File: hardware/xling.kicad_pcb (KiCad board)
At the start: 2 copper layers, 51 x 68 mm, 59 parts, among them J2 TPS63031, J3 MCP73831, J4 USB_OTG, J5 AVR ISP, J6 Battery, Q1 TP0610T, SW1 Reset, SW2 Up, SW3 Select, SW4 Down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

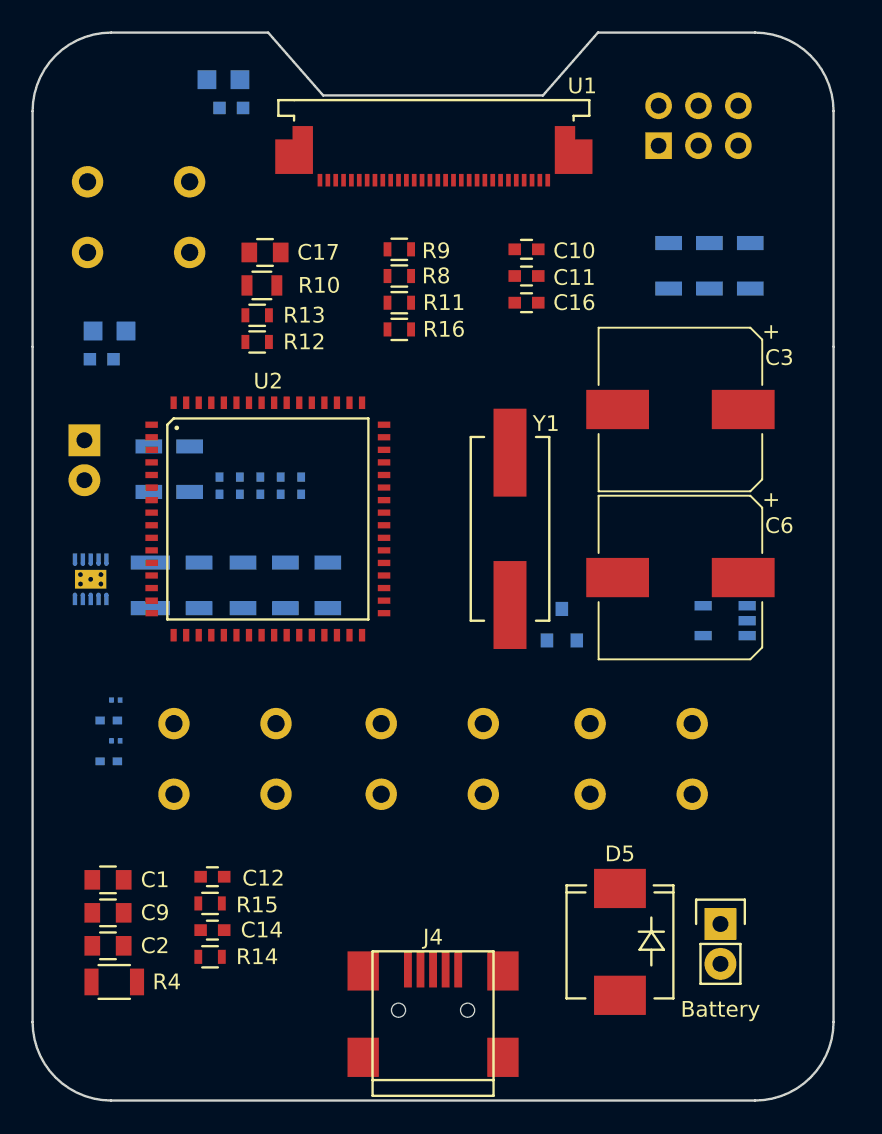
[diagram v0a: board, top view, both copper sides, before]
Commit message: patch 0.1.8: Add other OLED and DCDC 3V-to-12V.
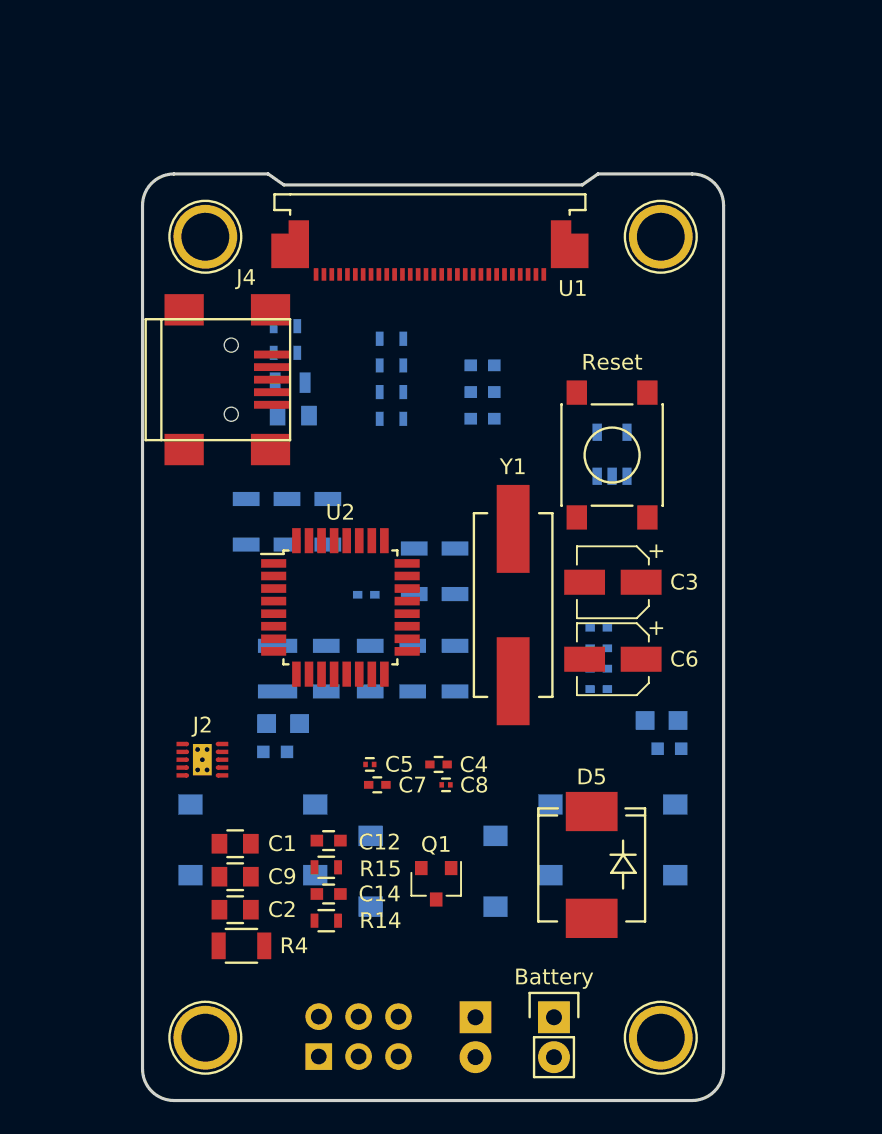
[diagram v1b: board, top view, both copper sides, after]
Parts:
- added REF**: 1pin, Connectors:1pin, F.Cu at (123.0, 134.0)
- added REF**: 1pin, Connectors:1pin, F.Cu at (152.0, 134.0)
- added REF**: 1pin, Connectors:1pin, F.Cu at (123.0, 83.0)
- added REF**: 1pin, Connectors:1pin, F.Cu at (152.0, 83.0)
- C10, C11, C16, C17, R10, R11, R12, R13, R16, R8, R9: moved to B.Cu
- C3, C6: footprint Capacitors_SMD:CP_Elec_10x10 -> Capacitors_SMD:CP_Elec_4x5.3
- C4, C5, C7, C8, J2, Q1: moved to F.Cu
- J5: footprint Socket_Strips:Socket_Strip_Angled_2x03_Pitch2.54mm -> Socket_Strips:Socket_Strip_Straight_2x03_Pitch2.54mm
- SW1: footprint Buttons_Switches_THT:SW_PUSH_6mm -> Buttons_Switches_SMD:SW_SPST_PTS645; moved to F.Cu
- SW2, SW3, SW4: footprint Buttons_Switches_THT:SW_PUSH_6mm -> Buttons_Switches_SMD:SW_SPST_PTS645
- U2: value ATMEGA128-16AU -> ATMEGA328P-AU; footprint Xling Footprints:ATmega128_64-lead_14x14x1.0mm_TQFP -> Housings_QFP:TQFP-32_7x7mm_Pitch0.8mm
- moved J5 61.9 mm to (130.2, 135.2)
- moved D1 49.4 mm to (152.6, 115.6)
- moved D2 49.4 mm to (152.1, 113.8)
- moved JP1 44.4 mm to (140.2, 132.7)
- moved J4 43.2 mm to (123.8, 92.1), turned to 0 degrees
- moved SW1 32.0 mm to (148.9, 96.9), turned to 90 degrees
- moved R3 31.5 mm to (128.2, 101.2)
- moved R6 31.5 mm to (125.6, 101.2)
- moved R7 31.5 mm to (130.8, 101.2)
- moved D3 27.3 mm to (128.0, 114.0)
- moved D4 27.3 mm to (127.5, 115.8)
- moved C15 26.3 mm to (148.1, 111.8), turned to 180 degrees
- moved C18 24.5 mm to (148.1, 110.5), turned to 180 degrees
- moved C19 22.7 mm to (148.1, 109.2), turned to 180 degrees
- moved C8 21.2 mm to (138.3, 117.9)
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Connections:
- R8 pad 2: /OLED_SCL -> /OLED_SDA
- R9 pad 2: /OLED_SDA -> /OLED_SCL
- U2 pad 11: /ISP_SCK -> Net-(U2-Pad11)
- U2 pad 15: Net-(U2-Pad15) -> /ISP_PDI_MOSI
- U2 pad 16: Net-(U2-Pad16) -> /ISP_PDO_MISO
- U2 pad 17: Net-(U2-Pad17) -> /ISP_SCK
- U2 pad 18: Net-(U2-Pad18) -> +3V3
- U2 pad 2: Net-(R11-Pad1) -> Net-(U2-Pad2)
- U2 pad 20: /ISP_RST -> GND
- U2 pad 21: +3V3 -> GND
- U2 pad 22: GND -> Net-(U2-Pad22)
- U2 pad 23: Net-(C13-Pad1) -> Net-(U2-Pad23)
- U2 pad 24: Net-(C15-Pad1) -> Net-(U2-Pad24)
- U2 pad 25: /OLED_SCL -> Net-(U2-Pad25)
- U2 pad 26: /OLED_SDA -> Net-(U2-Pad26)
- U2 pad 27: Net-(U2-Pad27) -> /OLED_SDA
- U2 pad 28: Net-(U2-Pad28) -> /OLED_SCL
- U2 pad 29: Net-(U2-Pad29) -> /ISP_RST
- U2 pad 3: /ISP_PDO_MISO -> GND
- U2 pad 30: Net-(U2-Pad30) -> /BTN1
- U2 pad 31: Net-(U2-Pad31) -> /BTN2
- U2 pad 32: Net-(U2-Pad32) -> /BTN3
- U2 pad 4: Net-(U2-Pad4) -> +3V3
- U2 pad 5: Net-(U2-Pad5) -> GND
- U2 pad 6: Net-(D3-Pad1) -> +3V3
- U2 pad 7: Net-(D4-Pad1) -> Net-(C13-Pad1)
- U2 pad 8: Net-(U2-Pad8) -> Net-(C15-Pad1)
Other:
- board size 51 x 68 mm -> 37 x 59 mm
- net class Default: clearance 0.25 -> 0.21
- rule trace_clearance: 0.25 -> 0.21
- rule trace_min: 0.2 -> 0.25
- rule via_min_size: 0.4 -> 0.6

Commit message: patch 0.1.10: First PCB prototype.
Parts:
- removed C14, C16: 2.2uF, Capacitors_SMD:C_0603
- removed C17, C2, C9: 10uF, Capacitors_SMD:C_0805
- removed C4: 10nF, Capacitors_SMD:C_0402
- removed D4: amber, LEDs:LED_0603
- removed J2: TPS63031, Xling Footprints:TPS63031_QFN_10
- removed JP1: D2D1, Pin_Headers:Pin_Header_Straight_1x02
- removed R10: 174K, Resistors_SMD:R_0805
- removed R11, R12, R13: 1K, Resistors_SMD:R_0603
- removed the REF** at (152.0, 134.0)
- removed the REF** at (123.0, 83.0)
- removed the REF** at (152.0, 83.0)
- removed SW1: Reset, Buttons_Switches_SMD:SW_SPST_PTS645
- added L2: 22uH, Inductors_SMD:L_7.3x7.3_H3.5, F.Cu at (127.1, 115.2)
- added REF**: 1pin, Connectors:1pin, F.Cu at (160.0, 134.0)
- added REF**: 1pin, Connectors:1pin, F.Cu at (160.0, 82.0)
- added REF**: 1pin, Connectors:1pin, F.Cu at (123.0, 82.0)
- added U3: DEP_128064I, Xling Footprints:XF2M_24151AR100_SMD_1x24_Pitch_0.5mm, F.Cu at (141.5, 81.2)
- added U4: MCP1640B-CH, TO_SOT_Packages_SMD:SOT-23-6, B.Cu at (141.7, 93.0)
- C1, J4, Q1: moved to B.Cu
- C10: value 2.2uF -> 33uF; footprint Capacitors_SMD:C_0603 -> Capacitors_Tantalum_SMD:CP_Tantalum_Case-C_EIA-6032-28_Reflow; moved to F.Cu
- C11, C13, J3, J5, R1, R16, R3, R5, R9: moved to F.Cu
- C5: value 0.1uF -> 4.7uF; moved to B.Cu
- D3: value green -> 1N5818; footprint LEDs:LED_0805 -> Diodes_THT:D_DO-41_SOD81_P7.62mm_Horizontal; moved to F.Cu
- D5: value B320 -> 1N5818; footprint Diodes_SMD:SMC_Standard -> Diodes_THT:D_DO-41_SOD81_P7.62mm_Horizontal
- L1: value 1.5uH -> 4.7uH
- R2: value 100K -> 910K
- R6: value 10K -> 191K; footprint Resistors_SMD:R_1206 -> Resistors_SMD:R_0805
- R7: value 10K -> 110K; footprint Resistors_SMD:R_1206 -> Resistors_SMD:R_0805
- U1: value SH1106G -> LT1109CZ-12; footprint Xling Footprints:Connector_FFC_FPC_MOLEX_524353071_30-pins -> TO_SOT_Packages_THT:TO-92_Inline_Narrow_Oval
- moved J5 47.9 mm to (152.4, 92.8), turned to 0 degrees
- moved J4 44.6 mm to (141.5, 133.0), turned to 90 degrees
- moved D5 36.2 mm to (156.8, 88.0)
- moved C1 35.0 mm to (145.1, 93.1), turned to 90 degrees
- moved R3 27.9 mm to (154.2, 111.2), turned to 180 degrees
- moved C18 26.0 mm to (127.5, 94.6)
- moved C19 24.3 mm to (127.5, 96.4)
- moved C5 23.9 mm to (138.8, 93.3), turned to 90 degrees
- moved R16 21.6 mm to (138.3, 110.8)
- moved C15 21.4 mm to (127.5, 105.9)
- moved D3 21.0 mm to (130.4, 93.1), turned to 90 degrees
- moved R1 20.7 mm to (159.2, 100.3), turned to 180 degrees
- moved R6 19.5 mm to (144.8, 97.6), turned to 180 degrees
- moved R14 19.1 mm to (149.3, 122.2)
- moved L1 19.1 mm to (136.0, 93.4)
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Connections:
- C10 pad 1: Net-(C10-Pad1) -> +12V
- C10 pad 2: Net-(C10-Pad2) -> GND
- C11 pad 2: Net-(C11-Pad2) -> GND
- C12 pad 1: +3V3 -> +12V
- D3 pad 1: Net-(D3-Pad1) -> +12V
- D5 pad 1: Net-(D5-Pad1) -> Net-(C5-Pad1)
- L1 pad 1: Net-(J2-Pad4) -> Net-(C5-Pad1)
- Q1 pad 2: Net-(D5-Pad1) -> Net-(C5-Pad1)
- R2 pad 1: Net-(C4-Pad1) -> GND
- R2 pad 2: Net-(D5-Pad1) -> Net-(R2-Pad2)
- R6 pad 2: /ISP_RST -> Net-(R6-Pad2)
- R7 pad 1: +3V3 -> Net-(R6-Pad2)
- U1 pad 2: Net-(C10-Pad1) -> Net-(D3-Pad2)
- U1 pad 3: Net-(C10-Pad2) -> +12V
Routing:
- net GND: track 0.00 -> 368.6 mm, vias 0 -> 15
- net +3V3: track 0.00 -> 134.9 mm, vias 0 -> 7
- net +12V: track 0.00 -> 84.2 mm, vias 0 -> 6
- net Net-(C3-Pad1): track 0.00 -> 75.7 mm, vias 0 -> 1
- net /ISP_RST: track 0.00 -> 48.4 mm, vias 0 -> 2
- net Net-(C5-Pad1): track 0.00 -> 46.7 mm
- net /ISP_PDO_MISO: track 0.00 -> 44.5 mm, vias 0 -> 2
- net Net-(R14-Pad2): track 0.00 -> 43.5 mm, vias 0 -> 3
- net /ISP_SCK: track 0.00 -> 38.9 mm, vias 0 -> 2
- net Net-(C6-Pad1): track 0.00 -> 37.7 mm, vias 0 -> 1
- net Net-(R15-Pad2): track 0.00 -> 37.6 mm, vias 0 -> 2
- net /OLED_SDA: track 0.00 -> 33.3 mm, vias 0 -> 1
- net Net-(D3-Pad2): track 0.00 -> 33.2 mm
- net Net-(R16-Pad2): track 0.00 -> 32.5 mm, vias 0 -> 3
- net Net-(R2-Pad2): track 0.00 -> 31.8 mm, vias 0 -> 1
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- added copper zone on B.Cu, net +3V3
- added copper zone on B.Cu, net GND
- added copper zone on F.Cu, net GND
- added copper zone on F.Cu, net Net-(C3-Pad1)
- added copper zone on B.Cu, net Net-(C5-Pad1)
- added copper zone on F.Cu, net Net-(C6-Pad1)
- added copper zone on B.Cu, net Net-(L1-Pad2)
- added copper zone on B.Cu, net Net-(R6-Pad2)
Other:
- board size 37 x 59 mm -> 45 x 60 mm

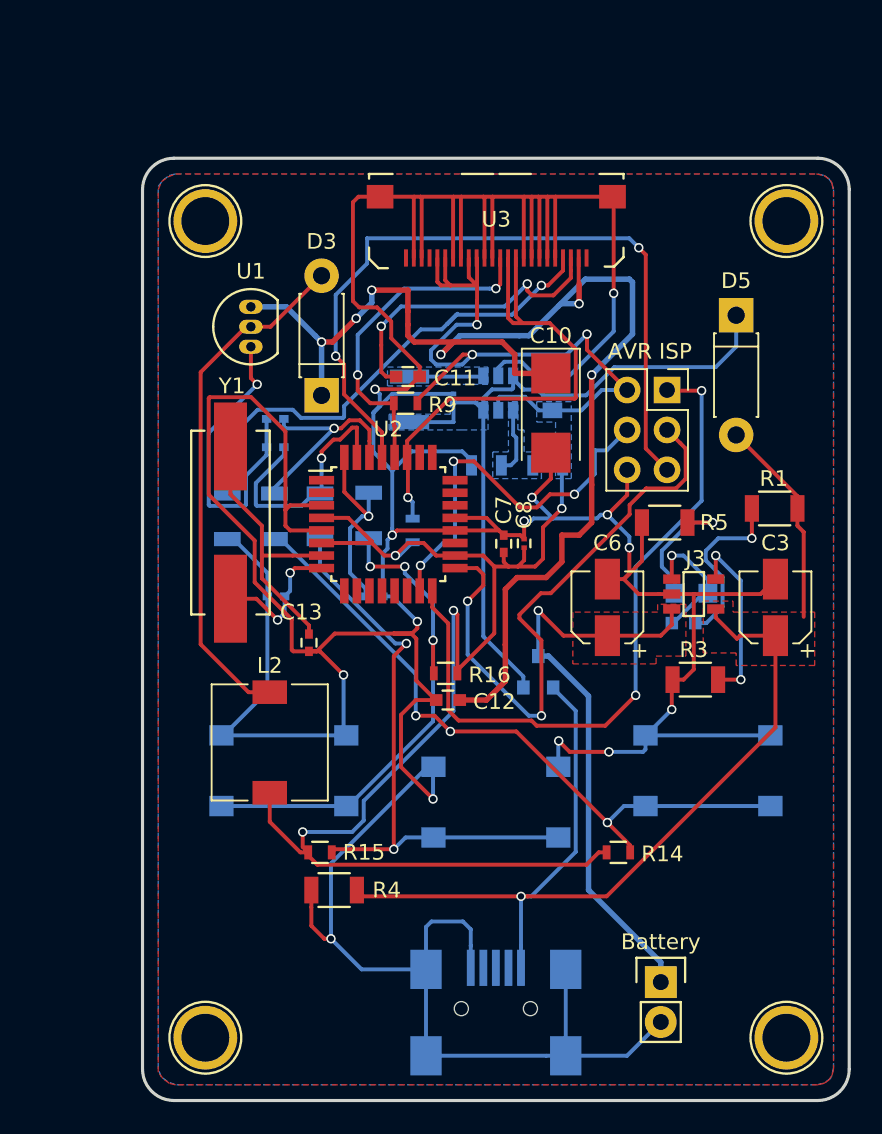
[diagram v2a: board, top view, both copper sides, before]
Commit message: patch 0.1.11: Add OSHW and 1KIB logos to the PCB.
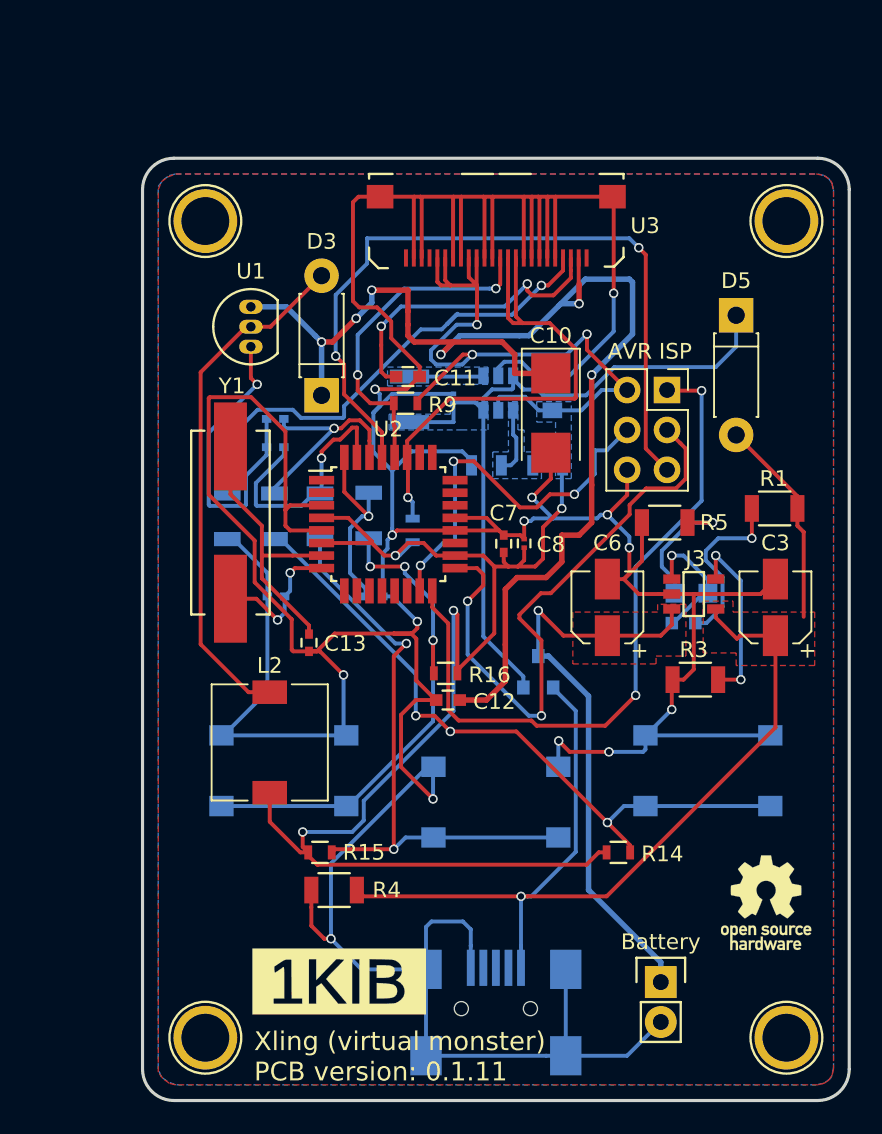
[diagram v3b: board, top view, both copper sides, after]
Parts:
- added G***: LOGO, Xling Footprints:1KIB_Logo_11.0x4.2mm_SilkScreen, F.Cu at (131.5, 130.4)
- added REF***: OSHW-Logo_5.7x6mm_SilkScreen, Symbols:OSHW-Logo_5.7x6mm_SilkScreen, F.Cu at (158.7, 125.4)
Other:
- board text added: "Xling (virtual monster) PCB version: 0.1.11"
